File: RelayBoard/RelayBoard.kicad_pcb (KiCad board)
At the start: 2 copper layers, 96.3 x 38.1 mm, 67 parts, among them J1 Micro_SD_Card, J10 Conn_01x04_Male, J11 Conn_01x04_Male, J13 Conn_01x04_Male, J2 Screw_Terminal_01x02, J3 Conn_01x04_Male, J4 Conn_01x04_Male, J5 Conn_01x04_Male, J7 SI-52008-F, J8 SI-52008-F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

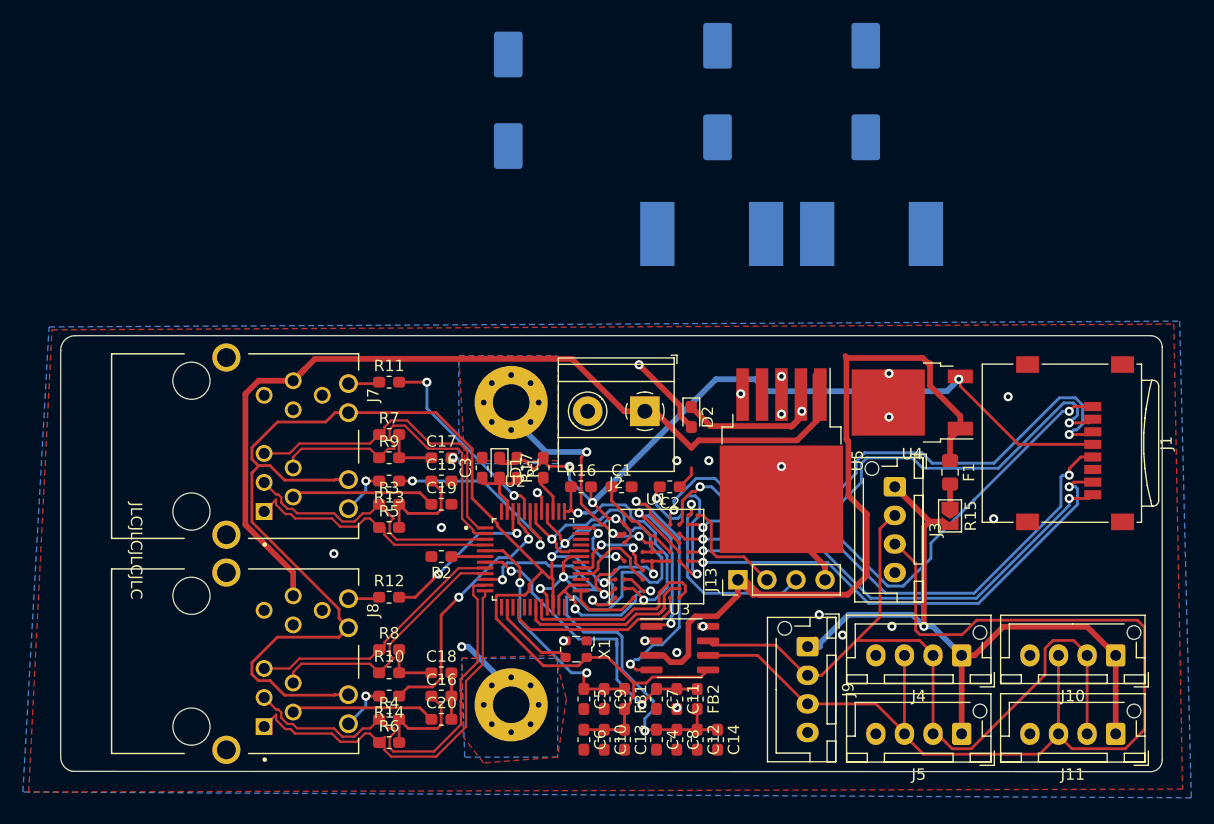
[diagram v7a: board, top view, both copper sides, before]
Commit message: ok give up on trying to regulate 24 to 5
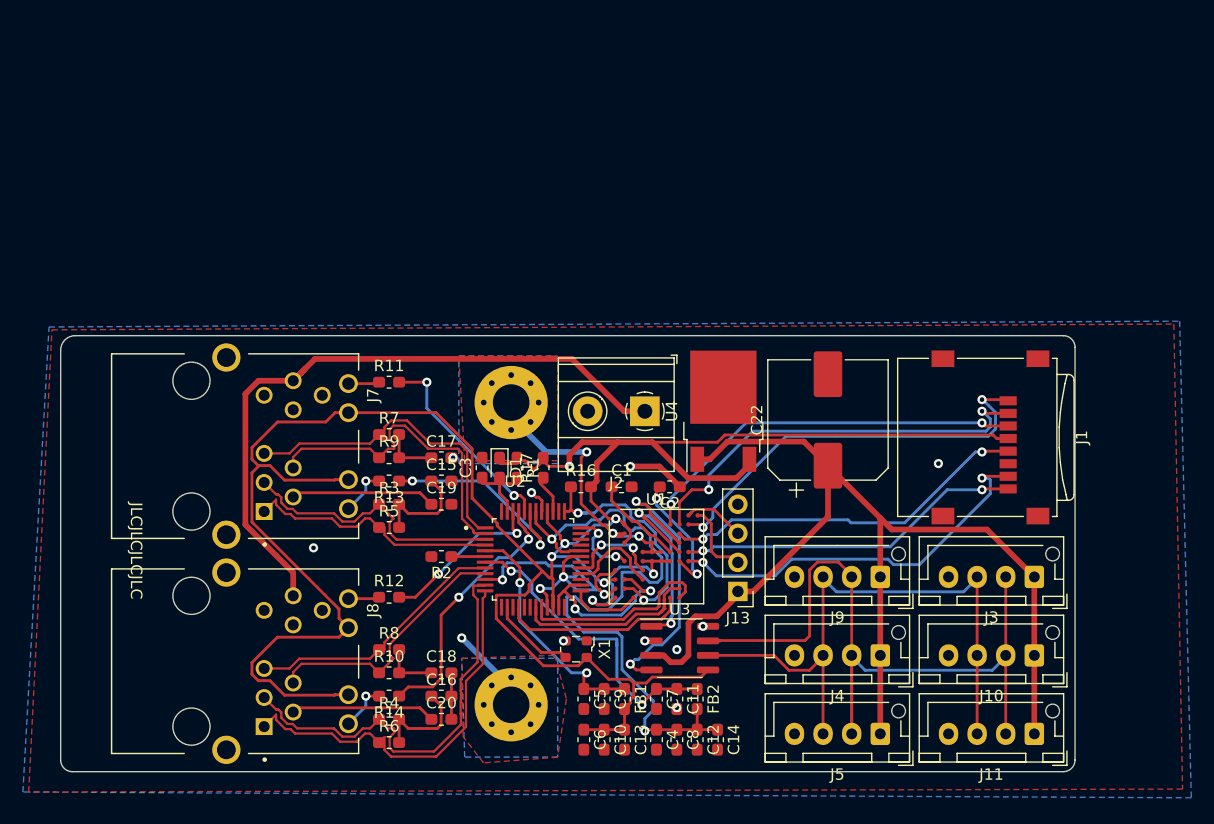
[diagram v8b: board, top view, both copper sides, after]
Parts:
- removed C21, C23: 470uF EMZS350ARA471MHA0G, Capacitor_SMD:CP_Elec_10x10
- removed D2: CCS15F40L3FTR-ND, Diode_SMD:D_0603_1608Metric_Pad1.05x0.95mm_HandSolder
- removed F1: 1A, Fuse:Fuse_0805_2012Metric_Pad1.15x1.40mm_HandSolder
- removed L1: 330uH PA4320, Inductor_SMD:L_Pulse_PA4320
- removed L2: 22uH PA4320, Inductor_SMD:L_Pulse_PA4320
- removed R15: 0Ω, Jumper:SolderJumper-2_P1.3mm_Open_TrianglePad1.0x1.5mm
- removed U5: LM2575-5.0BU, Package_TO_SOT_SMD:TO-263-5_TabPin3
- C22: moved to F.Cu
- moved C22 30.3 mm to (158.2, 68.8)
- moved U4 16.5 mm to (149.1, 68.1), turned to 90 degrees
- moved J3 14.5 mm to (176.3, 82.5), turned to 180 degrees
- moved J9 8.80 mm to (162.8, 82.5), turned to 180 degrees
- moved J1 7.41 mm to (172.4, 70.4)
- moved J10 7.11 mm to (176.3, 89.4)
- moved J11 7.11 mm to (176.3, 96.3)
- moved J4 7.11 mm to (162.8, 89.4)
- moved J5 7.11 mm to (162.8, 96.3)
- moved J13 1.02 mm to (150.4, 83.8), turned to 180 degrees
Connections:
- C22 pad 1: Net-(C22-Pad1) -> 5V
- J10 pad 1: 5V_CAN -> 5V
- J11 pad 1: 5V_CAN -> 5V
- J3 pad 1: 5V_CAN -> 5V
- J4 pad 1: 5V_CAN -> 5V
- J5 pad 1: 5V_CAN -> 5V
- J9 pad 1: 5V_CAN -> 5V
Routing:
- net 5V_CAN: track 61.6 -> 0.00 mm, vias 1 -> 0
- net CANL: track 95.8 -> 53.7 mm
- net 24V: track 82.6 -> 59.8 mm
- net 5V: track 72.0 -> 94.5 mm
- net SD_CMD: track 50.3 -> 34.7 mm
- net Net-(D2-Pad1): track 14.2 -> 0.00 mm, vias 1 -> 0
- net SD_CLK: track 45.0 -> 32.3 mm
- net SWCLK: track 18.2 -> 5.75 mm, vias 1 -> 0
- net SD_D3: track 48.3 -> 36.7 mm
- net SD_D1: track 41.3 -> 30.2 mm
- net SD_D2: track 45.7 -> 36.3 mm
- net SD_D0: track 43.7 -> 34.6 mm
- net GND: track 88.5 -> 80.1 mm, vias 31 -> 18
- net Net-(C2-Pad2): track 16.5 -> 11.2 mm
- net SWDIO: track 9.81 -> 6.96 mm
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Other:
- board size 96.3 x 38.1 mm -> 88.6 x 38.1 mm
